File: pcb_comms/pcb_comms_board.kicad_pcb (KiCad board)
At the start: 2 copper layers, 90 x 90.2 mm, 83 parts, among them IC1 LDL1117S33R, IC2 TPS2553QDBVRQ1, IC4 BGS12WN6E6329XTSA1, J1 Conn_01x06_Pin, J2 Conn_02x20_Counter_Clockwise, J3 Conn_02x08_Counter_Clockwise, J4 SMA_CONN, J5 SMA_CONN, J7 USB-B-Micro, U2 STM32WLE5CCU6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

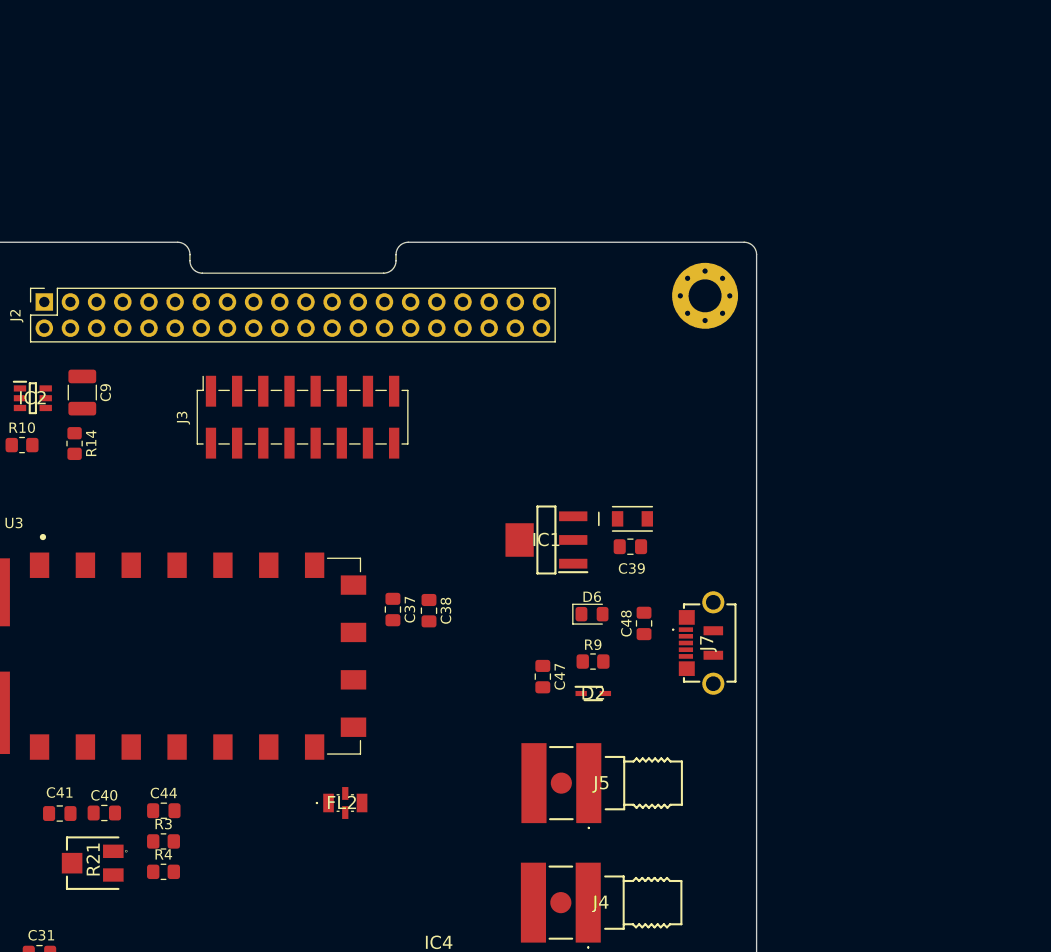
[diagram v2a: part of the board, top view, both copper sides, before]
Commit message: Update schematic. Add net classes and JST footprints for aux
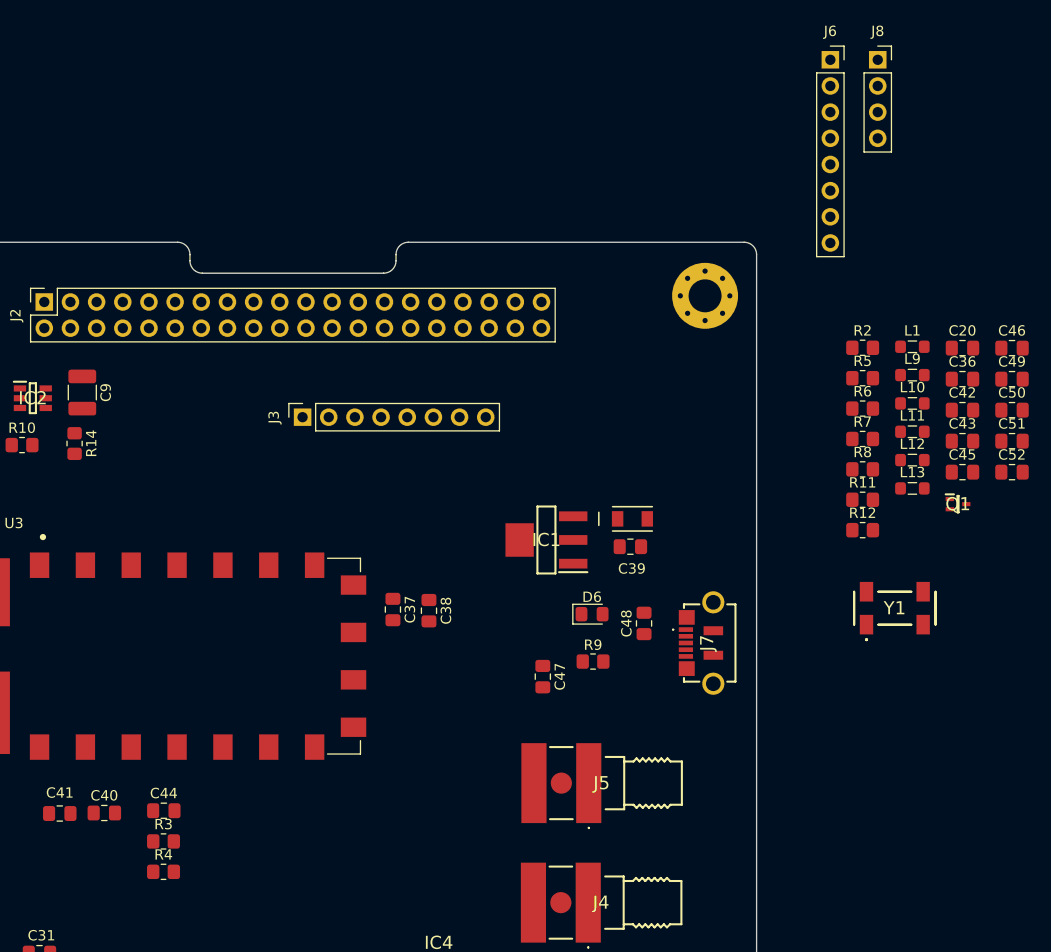
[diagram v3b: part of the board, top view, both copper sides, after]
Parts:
- removed D2: AQ3530-01FTG, ESD_PROTECTION_DIODE_AQ3530-01FTG:ESD_PROTECTION_DIODE_AQ3530-01FTG
- removed FL2: LFCN-160+, RF_FILTER_LFCN-160+:RF_FILTER_LFCN-160+
- removed R21: 3314J-1-103E, TRIMPOT_10K_3314J-1-103E:TRIMPOT_10K_3314J-1-103E
- added C20: 1uF, Capacitor_SMD:C_0805_2012Metric_Pad1.18x1.45mm_HandSolder, F.Cu at (211.2, 56.4)
- added C36: 1nF, Capacitor_SMD:C_0805_2012Metric_Pad1.18x1.45mm_HandSolder, F.Cu at (211.2, 59.4)
- added C42: 1nF, Capacitor_SMD:C_0805_2012Metric_Pad1.18x1.45mm_HandSolder, F.Cu at (211.2, 62.4)
- added C43: 0.1uF, Capacitor_SMD:C_0805_2012Metric_Pad1.18x1.45mm_HandSolder, F.Cu at (211.2, 65.5)
- added C45: 1nF, Capacitor_SMD:C_0805_2012Metric_Pad1.18x1.45mm_HandSolder, F.Cu at (211.2, 68.5)
- added C46: 10uF, Capacitor_SMD:C_0805_2012Metric_Pad1.18x1.45mm_HandSolder, F.Cu at (216.0, 56.4)
- added C49: 10uF, Capacitor_SMD:C_0805_2012Metric_Pad1.18x1.45mm_HandSolder, F.Cu at (216.0, 59.4)
- added C50: 36pF, Capacitor_SMD:C_0805_2012Metric_Pad1.18x1.45mm_HandSolder, F.Cu at (216.0, 62.4)
- added C51: 36pF, Capacitor_SMD:C_0805_2012Metric_Pad1.18x1.45mm_HandSolder, F.Cu at (216.0, 65.5)
- added C52: 20pF, Capacitor_SMD:C_0805_2012Metric_Pad1.18x1.45mm_HandSolder, F.Cu at (216.0, 68.5)
- added J6: AUX1, Connector_PinSocket_2.54mm:PinSocket_1x08_P2.54mm_Vertical, F.Cu at (198.4, 28.4)
- added J8: AUX3, Connector_PinSocket_2.54mm:PinSocket_1x04_P2.54mm_Vertical, F.Cu at (203.0, 28.4)
- added L1: 1uH, Inductor_SMD:L_0805_2012Metric_Pad1.05x1.20mm_HandSolder, F.Cu at (206.3, 56.3)
- added L10: 1uH, Inductor_SMD:L_0805_2012Metric_Pad1.05x1.20mm_HandSolder, F.Cu at (206.3, 61.8)
- added L11: 56nH, Inductor_SMD:L_0805_2012Metric_Pad1.05x1.20mm_HandSolder, F.Cu at (206.3, 64.5)
- added L12: 68nH, Inductor_SMD:L_0805_2012Metric_Pad1.05x1.20mm_HandSolder, F.Cu at (206.3, 67.3)
- added L13: 56nH, Inductor_SMD:L_0805_2012Metric_Pad1.05x1.20mm_HandSolder, F.Cu at (206.3, 70.0)
- added L9: 1uH, Inductor_SMD:L_0805_2012Metric_Pad1.05x1.20mm_HandSolder, F.Cu at (206.3, 59.0)
- added Q1: DTC144EET1G, TRANSISTOR_DTC144EET1G:TRANSISTOR_DTC144EET1G, F.Cu at (210.8, 71.6)
- added R11: 10K, Resistor_SMD:R_0805_2012Metric_Pad1.20x1.40mm_HandSolder, F.Cu at (201.5, 71.1)
- added R12: 100, Resistor_SMD:R_0805_2012Metric_Pad1.20x1.40mm_HandSolder, F.Cu at (201.5, 74.1)
- added R2: 10K, Resistor_SMD:R_0805_2012Metric_Pad1.20x1.40mm_HandSolder, F.Cu at (201.5, 56.4)
- added R5: 1K, Resistor_SMD:R_0805_2012Metric_Pad1.20x1.40mm_HandSolder, F.Cu at (201.5, 59.3)
- added R6: 10K, Resistor_SMD:R_0805_2012Metric_Pad1.20x1.40mm_HandSolder, F.Cu at (201.5, 62.3)
- added R7: 10K, Resistor_SMD:R_0805_2012Metric_Pad1.20x1.40mm_HandSolder, F.Cu at (201.5, 65.2)
- added R8: 10K, Resistor_SMD:R_0805_2012Metric_Pad1.20x1.40mm_HandSolder, F.Cu at (201.5, 68.2)
- added Y1: G43270018, CRYSTAL_32.687KHz_G43270018:CRYSTAL_32.687KHz_G43270018, F.Cu at (204.6, 81.7)
- C37: value 0.1uF -> 220nF
- C38: value 4.7uF -> 20pF
- C40: value 0.1uF -> 220pF
- C41: value 4.7uF -> 220nF
- J2: value Conn_02x20_Counter_Clockwise -> Conn_02x20_Odd_Even
- J3: value Conn_02x08_Counter_Clockwise -> AUX2; footprint Connector_PinSocket_2.54mm:PinSocket_2x08_P2.54mm_Vertical_SMD -> Connector_PinSocket_2.54mm:PinSocket_1x08_P2.54mm_Vertical
- R14: value 88.7K -> 26.1K
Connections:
- net /RF/MIC_IN renamed /APRS_RADIO/MIC_IN
- net DRA_RX_UART1 renamed DRA_RX_UART1_TX
- net DRA_TX_UART1 renamed DRA_TX_UART1_RX
- net Net-(D6-K) renamed /OCP/D6_TO_R9
- net Net-(IC2-ILIM) renamed /OCP/ILIM
- net Net-(R21-WIPER) renamed /APRS_RADIO/MIC_IN1
- C37 pad 1: VBAT -> /APRS_RADIO/AF_OUT
- C37 pad 2: GND -> /APRS_RADIO/AF_OUT2
- C38 pad 1: VBAT -> /APRS_RADIO/DRA_ANT_NO_FILTER
- C44 pad 2: Net-(U3-AF_OUT) -> /APRS_RADIO/AF_OUT2
- C48 pad 1: +3.3V -> VBAT
- D6 pad 2: +3.3V -> VBAT
- IC1 pad 4: +3.3V -> VBAT
- J2 pad 23: SPI1_MISO -> SPI1_SCK
- J2 pad 24: SPI1_SCK -> SPI1_MISO
- J2 pad 25: SPI1_CS -> SPI1_MOSI
- J2 pad 26: SPI1_MOSI -> SPI1_CS
- J2 pad 29: unconnected-(J2-Pin_29-Pad29) -> OCP_EN
- J2 pad 30: OCP_EN -> unconnected-(J2-Pin_30-Pad30)
- J2 pad 36: unconnected-(J2-Pin_36-Pad36) -> GND
- J2 pad 6: unconnected-(J2-Pin_6-Pad6) -> VBAT_IN
- J2 pad 7: unconnected-(J2-Pin_7-Pad7) -> GND
- J2 pad 8: unconnected-(J2-Pin_8-Pad8) -> GND
- J3 pad 1: AUX0_SDA -> I2C2_SCL
- J3 pad 2: AUX1_SCL -> GND
- J3 pad 3: AUX2 -> I2C2_SDA
- J3 pad 4: AUX3 -> GND
- J3 pad 5: AUX4 -> AUX2
- J3 pad 6: AUX5 -> GND
- J3 pad 7: unconnected-(J3-Pin_7-Pad7) -> AUX3
- J3 pad 8: unconnected-(J3-Pin_8-Pad8) -> GND
- J5 pad 3: /RF/DRA_ANT -> /APRS_RADIO/DRA_ANT
- R4 pad 2: VBAT -> /APRS_RADIO/3V3_DRA
- U2 pad 10: TX_UART2 -> UART_RX
- U2 pad 13: DRA_PTT -> DRA_SQ_TO_STM32
- U2 pad 14: DRA_ENA -> STM32_TO_DRA_PTT
- U2 pad 15: AUX8 -> AUX1
- U2 pad 16: AUX7 -> AUX2
- U2 pad 17: AUX6 -> AUX3
- U2 pad 30: AUX5 -> AUX4
- U2 pad 31: AUX4 -> AUX5
- U2 pad 32: AUX3 -> STM32_TO_DRA_ENA
- U2 pad 35: AUX1_SCL -> I2C2_SCL
- U2 pad 38: AUX10 -> OCP_NFAULT
- U2 pad 39: OCP_NFAULT -> OSC_RTC_IN
- U2 pad 40: AUX2 -> OSC_RTC_OUT
- U2 pad 43: AUX0_SDA -> I2C2_SDA
- U2 pad 6: AUX9 -> AUX0
- U2 pad 9: RX_UART2 -> UART2_TX
- U3 pad 1: unconnected-(U3-SQ-Pad1) -> Net-(U3-SQ)
- U3 pad 12: /RF/DRA_ANT_NO_FILTER -> /APRS_RADIO/DRA_ANT_NO_FILTER
- U3 pad 3: Net-(U3-AF_OUT) -> /APRS_RADIO/AF_OUT
- U3 pad 5: DRA_PTT -> /APRS_RADIO/DRA_PTT
- U3 pad 6: DRA_ENA -> STM32_TO_DRA_ENA
- U3 pad 8: VBAT -> /APRS_RADIO/3V3_DRA

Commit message: Update pcb
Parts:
- J8: value AUX3 -> AUX2; footprint Connector_PinSocket_2.54mm:PinSocket_1x04_P2.54mm_Vertical -> Connector_PinSocket_2.54mm:PinSocket_1x08_P2.54mm_Vertical
- moved J6 117.5 mm to (109.6, 105.4)
- moved J8 110.6 mm to (160.5, 130.6), turned to 90 degrees
- moved J7 77.4 mm to (109.4, 90.5), turned to 90 degrees
- moved J3 74.7 mm to (114.9, 130.6)
- moved C43 71.0 mm to (140.2, 64.4), turned to -90 degrees
- moved Q1 70.2 mm to (140.8, 76.7)
- moved C46 67.4 mm to (149.1, 64.3), turned to -90 degrees
- moved C36 66.5 mm to (146.9, 76.6), turned to -90 degrees
- moved Y1 65.6 mm to (140.9, 97.2), turned to 90 degrees
- moved C45 65.5 mm to (145.8, 64.3), turned to -90 degrees
- moved R7 64.8 mm to (137.8, 76.7), turned to 90 degrees
- moved C49 64.2 mm to (152.0, 64.3), turned to -90 degrees
- moved CR1 63.5 mm to (117.1, 86.5), turned to 180 degrees
- moved L10 63.2 mm to (143.2, 64.4), turned to 90 degrees
- moved C48 60.9 mm to (119.4, 83.0)
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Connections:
- IC1 pad 2: unconnected-(IC1-VOUT_1-Pad2) -> VBAT
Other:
- copper layers 2 -> 4

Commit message: Route pcb
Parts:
- moved J8 46.1 mm to (114.5, 133.5)
- moved C41 44.3 mm to (135.5, 83.4)
- moved L1 44.3 mm to (138.3, 83.4), turned to -90 degrees
- moved C40 42.2 mm to (141.0, 83.5)
- moved C20 39.5 mm to (144.3, 83.5), turned to -90 degrees
- moved R2 39.1 mm to (147.1, 83.5)
- moved R5 39.1 mm to (149.9, 83.5)
- moved C14 38.9 mm to (122.5, 96.8), turned to 90 degrees
- moved J4 36.7 mm to (181.5, 119.9)
- moved L2 35.6 mm to (124.5, 96.8), turned to -90 degrees
- moved J5 35.1 mm to (181.6, 105.0)
- moved C11 32.1 mm to (123.1, 101.0), turned to 180 degrees
- moved C10 26.8 mm to (119.6, 113.4)
- moved C18 25.6 mm to (135.1, 114.9)
- moved C30 25.5 mm to (149.4, 128.0), turned to 0 degrees
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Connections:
- U2 pad 13: DRA_SQ_TO_STM32 -> AUX4
- U2 pad 14: STM32_TO_DRA_PTT -> AUX5
- U2 pad 30: AUX4 -> STM32_TO_DRA_PTT
- U2 pad 31: AUX5 -> DRA_SQ_TO_STM32
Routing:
- net VBAT: track 0.00 -> 149.4 mm
- net JTMS_SWDIO_TO_STM32: track 0.00 -> 107.9 mm, vias 0 -> 2
- net DRA_RX_UART1_TX: track 0.00 -> 94.3 mm, vias 0 -> 2
- net DRA_TX_UART1_RX: track 0.00 -> 91.3 mm, vias 0 -> 2
- net SPI1_SCK: track 0.00 -> 81.0 mm, vias 0 -> 1
- net SPI1_MOSI: track 0.00 -> 72.8 mm, vias 0 -> 1
- net SPI1_CS: track 0.00 -> 70.0 mm, vias 0 -> 1
- net SPI1_MISO: track 0.00 -> 64.4 mm, vias 0 -> 1
- net JTDO_SWO_TO_STM32: track 0.00 -> 62.5 mm, vias 0 -> 2
- net STM32_TO_DRA_ENA: track 0.00 -> 61.9 mm, vias 0 -> 2
- net /APRS_RADIO/MIC_IN: track 0.00 -> 58.2 mm
- net STM32_NRST: track 0.00 -> 55.6 mm, vias 0 -> 2
- net JTCK_SWCLK_TO_STM32: track 0.00 -> 51.8 mm, vias 0 -> 4
- net STM32_TO_DRA_PTT: track 0.00 -> 50.0 mm, vias 0 -> 2
- net OCP_EN: track 0.00 -> 46.9 mm, vias 0 -> 1
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
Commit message: Update route
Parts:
- removed J6: AUX1, Connector_PinSocket_2.54mm:PinSocket_1x08_P2.54mm_Vertical
- removed J8: AUX2, Connector_PinSocket_2.54mm:PinSocket_1x08_P2.54mm_Vertical
- added J9: GPS, Connector_JST:JST_SH_BM06B-SRSS-TB_1x06-1MP_P1.00mm_Vertical, F.Cu at (108.7, 101.4)
- H1, H2, H3, H4: footprint MountingHole:MountingHole_3.2mm_M3_Pad_Via -> MountingHole:MountingHole_3.2mm_M3_DIN965_Pad_TopBottom
- J3: value AUX2 -> AUX; footprint Connector_PinSocket_2.54mm:PinSocket_1x08_P2.54mm_Vertical -> JST B6B-XH-A-LF-SN-:CONN_B6B-XH-A_JST
- moved J1 49.7 mm to (108.6, 116.5)
- moved SB3 49.7 mm to (103.5, 120.4)
- moved CR2 40.4 mm to (113.7, 117.0), turned to -90 degrees
- moved C13 5.71 mm to (166.1, 119.7)
- moved C23 3.15 mm to (165.2, 130.0)
- moved C25 3.15 mm to (162.9, 129.9)
- moved C28 3.05 mm to (172.1, 130.1)
- moved C29 3.05 mm to (167.5, 130.1)
- moved L7 3.05 mm to (169.7, 130.2)
- moved J3 2.71 mm to (116.3, 131.6), turned to 0 degrees
- moved S1 2.01 mm to (120.2, 122.5)
- moved R1 1.85 mm to (131.4, 123.2)
- moved C12 1.79 mm to (125.0, 123.3)
- moved D3 1.79 mm to (127.8, 123.2)
- moved J5 1.41 mm to (181.6, 106.4)
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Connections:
- J3 pad 1: I2C2_SCL -> AUX0
- J3 pad 2: GND -> AUX1
- J3 pad 3: I2C2_SDA -> AUX2
- J3 pad 4: GND -> AUX3
- J3 pad 5: AUX2 -> AUX4
- J3 pad 6: GND -> AUX5
- U2 pad 13: AUX4 -> AUX1
- U2 pad 14: AUX5 -> AUX2
- U2 pad 15: AUX1 -> AUX3
- U2 pad 16: AUX2 -> AUX4
- U2 pad 17: AUX3 -> AUX5
- U2 pad 35: I2C2_SCL -> unconnected-(U2-PA12-Pad35)
- U2 pad 43: I2C2_SDA -> unconnected-(U2-PA15-Pad43)
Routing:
- net GND: track 0.00 -> 166.6 mm, vias 11 -> 80
- net VBAT: track 149.4 -> 283.0 mm, vias 0 -> 5
- net JTMS_SWDIO_TO_STM32: track 107.9 -> 37.5 mm
- net /MCU/VDDRF1V55: track 19.3 -> 69.4 mm, vias 0 -> 8
- net OCP_NFAULT: track 4.06 -> 46.7 mm, vias 1 -> 4
- net /APRS_RADIO/3V3_DRA: track 41.6 -> 67.7 mm
- net AUX1: track 0.00 -> 24.7 mm, vias 0 -> 1
- net /APRS_RADIO/DRA_ANT: track 3.13 -> 27.4 mm
- net JTDO_SWO_TO_STM32: track 62.5 -> 39.0 mm
- net AUX2: track 0.00 -> 23.2 mm, vias 0 -> 1
- net JTCK_SWCLK_TO_STM32: track 51.8 -> 29.0 mm, vias 4 -> 2
- net AUX3: track 0.00 -> 22.5 mm, vias 0 -> 1
- net AUX4: track 0.00 -> 21.6 mm, vias 0 -> 1
- net AUX5: track 0.00 -> 21.2 mm, vias 0 -> 1
- net STM32_NRST: track 55.6 -> 34.6 mm, vias 2 -> 0
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- added copper zone on B.Cu, net GND
- added copper zone on In1.Cu, net GND

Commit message: Version 1.1
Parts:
- removed J5: SMA_CONN, SMA_ANTENNA_CONSMA002-SMD-G:SMA_ANTENNA_CONSMA002-SMD-G
- added J6: SMA_CONNECTOR, SMA_ANTENNA_VERTICAL:LPRS_SMA_CONNECTOR, F.Cu at (180.9, 120.9)
- J4: value SMA_CONN -> SMA_CONNECTOR; footprint SMA_ANTENNA_CONSMA002-SMD-G:SMA_ANTENNA_CONSMA002-SMD-G -> SMA_ANTENNA_VERTICAL:LPRS_SMA_CONNECTOR
- moved IC1 27.4 mm to (109.4, 65.1), turned to -90 degrees
- moved J4 26.9 mm to (183.4, 92.7), turned to 0 degrees
- moved R9 1.49 mm to (116.2, 82.8), turned to 180 degrees
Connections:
- J4 pad 1: GND -> /APRS_RADIO/DRA_ANT
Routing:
- net +5V: track 10.9 -> 51.3 mm, vias 0 -> 2
- net VBAT: track 283.0 -> 303.0 mm, vias 5 -> 8
- net GND: track 166.6 -> 148.1 mm, vias 80 -> 77
- net /APRS_RADIO/DRA_ANT: track 27.4 -> 15.5 mm
- net VBAT_IN: track 36.8 -> 30.8 mm
- net VR_PA: track 21.6 -> 22.7 mm
- net /RF/SMA1: track 16.3 -> 17.3 mm
- net RF_CRL_TO_STM32: track 44.4 -> 44.0 mm, vias 4 -> 2
- added copper zone on F.Cu, net VBAT

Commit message: re arrange
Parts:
- removed C4, C5: 0.1uF, Capacitor_SMD:C_0805_2012Metric_Pad1.18x1.45mm_HandSolder
- removed J3: AUX, JST B6B-XH-A-LF-SN-:CONN_B6B-XH-A_JST
- removed Y1: G43270018, CRYSTAL_32.687KHz_G43270018:CRYSTAL_32.687KHz_G43270018
- C33: footprint Capacitor_SMD:C_0805_2012Metric_Pad1.18x1.45mm_HandSolder -> Capacitor_SMD:C_0603_1608Metric_Pad1.08x0.95mm_HandSolder
- moved SB3 70.3 mm to (171.1, 101.2), turned to 180 degrees
- moved J1 67.2 mm to (175.0, 106.3), turned to -90 degrees
- moved C33 63.1 mm to (170.5, 73.6), turned to 0 degrees
- moved C10 62.3 mm to (154.3, 62.3), turned to 90 degrees
- moved CR2 61.1 mm to (174.5, 111.3), turned to 180 degrees
- moved C26 58.5 mm to (178.7, 69.5), turned to -90 degrees
- moved R3 57.0 mm to (114.1, 125.5)
- moved C31 56.0 mm to (175.7, 66.3), turned to 180 degrees
- moved Y3 55.6 mm to (175.6, 69.6), turned to 90 degrees
- moved C1 54.6 mm to (154.7, 74.0)
- moved R4 54.6 mm to (116.5, 125.5), turned to -90 degrees
- moved C14 54.0 mm to (161.2, 59.1), turned to 0 degrees
- moved C34 53.9 mm to (171.5, 67.1), turned to 0 degrees
- moved R11 52.5 mm to (118.7, 125.6), turned to -90 degrees
- moved S1 51.7 mm to (171.9, 119.7), turned to 0 degrees
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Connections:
- C1 pad 2: VBAT -> +3V3
- C10 pad 1: VBAT -> /MCU/VLXSMPS
- C11 pad 1: VBAT -> /MCU/VLXSMPS
- C2 pad 2: VBAT -> +3V3
- C3 pad 2: VBAT -> +3V3
- C32 pad 1: VBAT -> +3V3
- C33 pad 1: VBAT -> +3V3
- C43 pad 1: VBAT -> +3V3
- C48 pad 1: VBAT -> +3V3
- C9 pad 1: VBAT -> +3V3
- CR2 pad 1: VBAT -> +3V3
- D6 pad 2: VBAT -> +3V3
- FB2 pad 2: VBAT -> +3V3
- IC1 pad 2: VBAT -> +3V3
- IC1 pad 4: VBAT -> +3V3
- IC2 pad 6: VBAT -> +3V3
- J9 pad 5: VBAT -> +3V3
- L10 pad 1: VBAT -> +3V3
- L2 pad 1: VBAT -> /MCU/VLXSMPS
- R19 pad 2: VBAT -> +3V3
- S1 pad 1: VBAT -> +3V3
- U2 pad 11: VBAT -> +3V3
- U2 pad 12: RF_CRL_TO_STM32 -> unconnected-(U2-PA4-Pad12)
- U2 pad 13: AUX1 -> unconnected-(U2-PA5-Pad13)
- U2 pad 14: AUX2 -> unconnected-(U2-PA6-Pad14)
- U2 pad 15: AUX3 -> unconnected-(U2-PA7-Pad15)
- U2 pad 16: AUX4 -> unconnected-(U2-PA8-Pad16)
- U2 pad 17: AUX5 -> RF_CRL_TO_STM32
- U2 pad 25: VBAT -> +3V3
- U2 pad 28: VBAT -> +3V3
- U2 pad 37: VBAT -> unconnected-(U2-VBAT-Pad37)
- U2 pad 39: OSC_RTC_IN -> unconnected-(U2-PC14-OSC32_IN-Pad39)
- U2 pad 40: OSC_RTC_OUT -> unconnected-(U2-PC15-OSC32_OUT-Pad40)
- U2 pad 44: VBAT -> +3V3
- U2 pad 46: VBAT -> +3V3
- U2 pad 47: VBAT -> /MCU/VLXSMPS
- U2 pad 6: AUX0 -> unconnected-(U2-PB8-Pad6)
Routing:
- net VBAT: track 303.0 -> 0.00 mm, vias 8 -> 0
- net DRA_RX_UART1_TX: track 95.5 -> 0.00 mm, vias 2 -> 0
- net DRA_TX_UART1_RX: track 92.3 -> 0.00 mm, vias 2 -> 0
- net SPI1_SCK: track 78.5 -> 0.00 mm, vias 1 -> 0
- net GND: track 148.1 -> 72.9 mm, vias 77 -> 176
- net SPI1_MOSI: track 73.0 -> 0.00 mm, vias 1 -> 0
- net SPI1_CS: track 69.6 -> 0.00 mm, vias 1 -> 0
- net +3V3: track 0.00 -> 68.7 mm, vias 0 -> 4
- net SPI1_MISO: track 64.4 -> 0.00 mm, vias 1 -> 0
- net /APRS_RADIO/MIC_IN: track 58.2 -> 3.49 mm
- net STM32_TO_DRA_ENA: track 61.7 -> 7.51 mm, vias 2 -> 0
- net /MCU/VDDRF1V55: track 69.4 -> 18.6 mm, vias 8 -> 0
- net STM32_TO_DRA_PTT: track 50.0 -> 2.19 mm, vias 2 -> 0
- net OCP_NFAULT: track 46.7 -> 1.21 mm, vias 4 -> 2
- net OCP_EN: track 46.9 -> 1.69 mm
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- added copper zone on F.Cu, net +3V3
- removed copper zone on F.Cu, net VBAT
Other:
- board text added: "C25"
